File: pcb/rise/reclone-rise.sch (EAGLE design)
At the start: 3 parts, among them U1 6SLX25FTG256

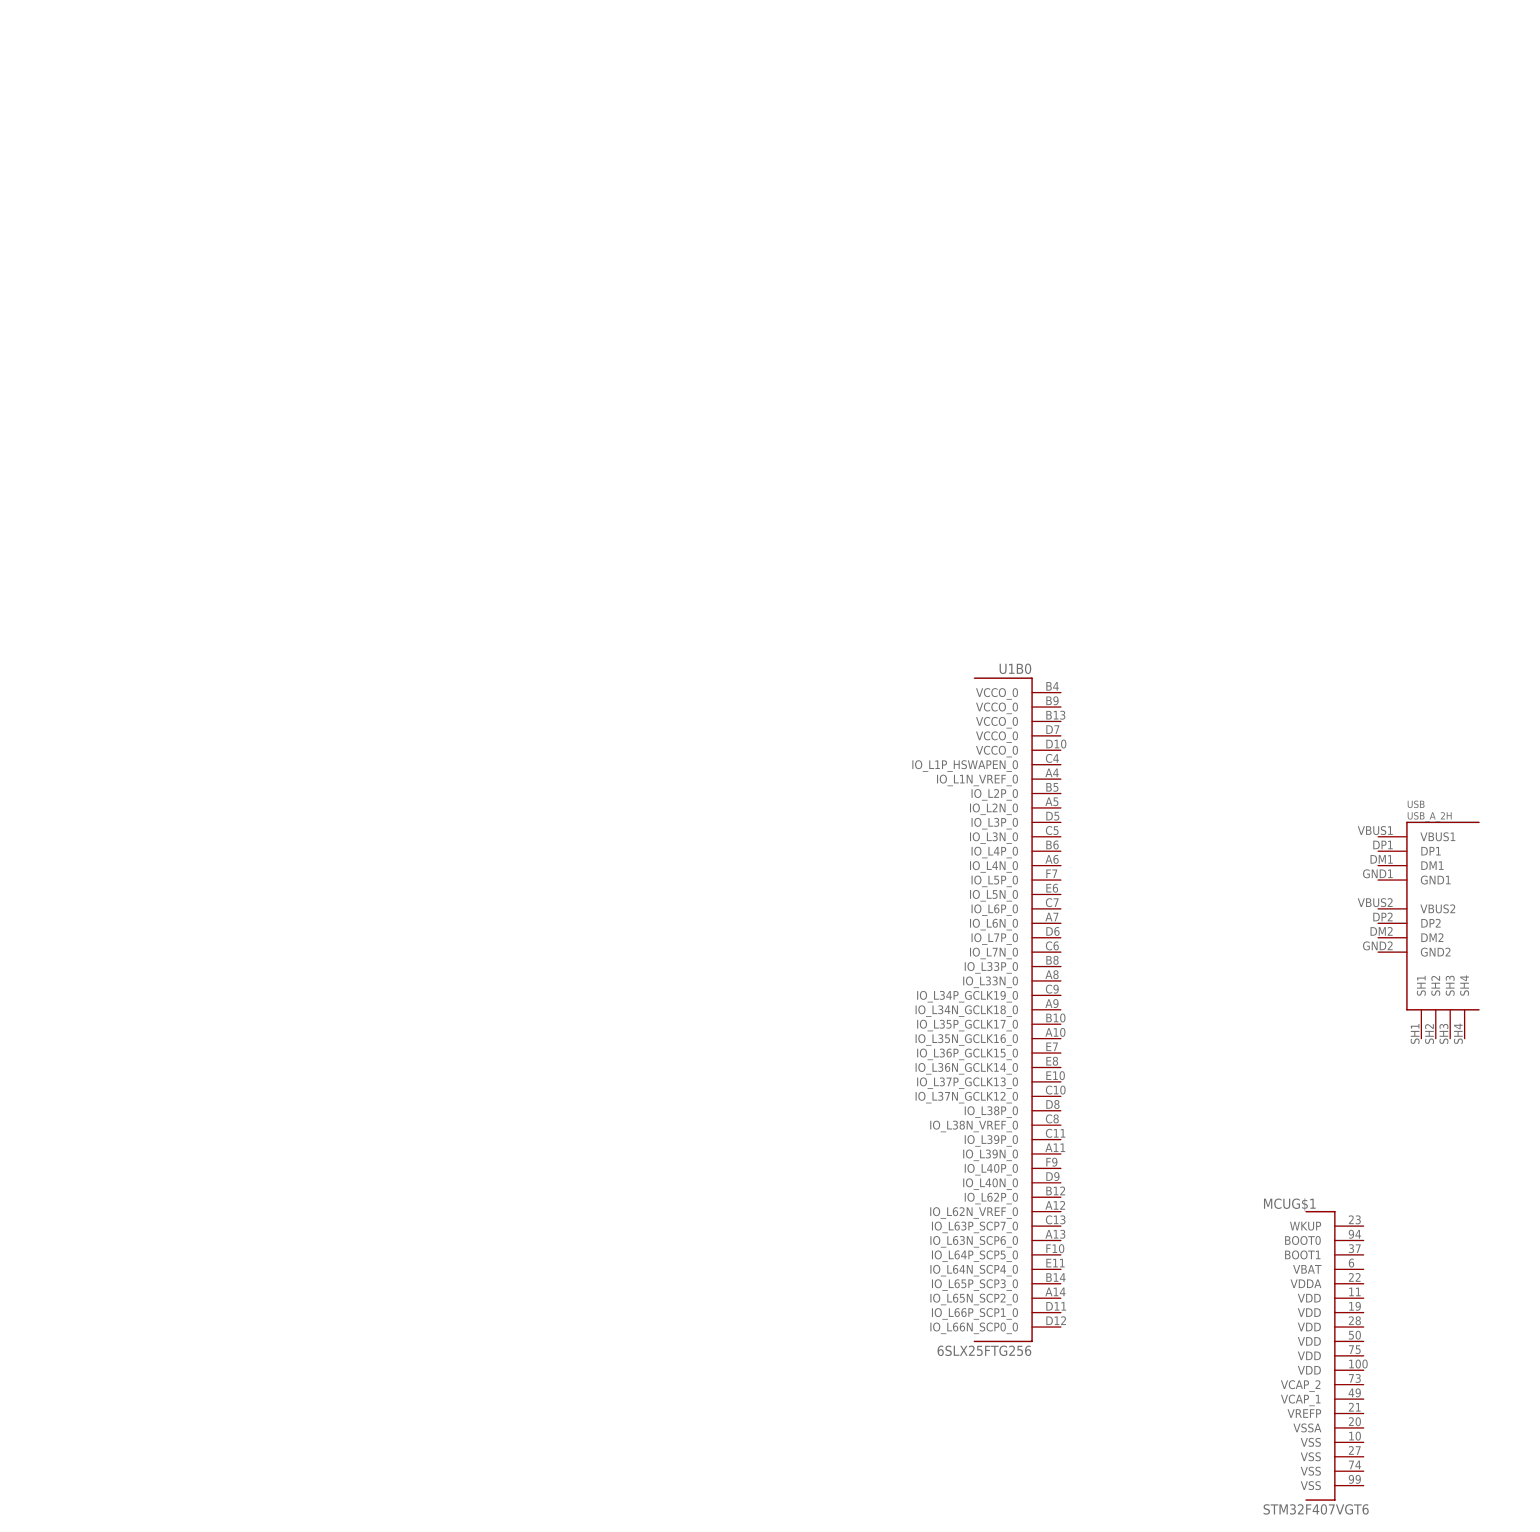
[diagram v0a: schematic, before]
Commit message: Added a ton of components just to get a sense for whether layout is possible on the top of the board
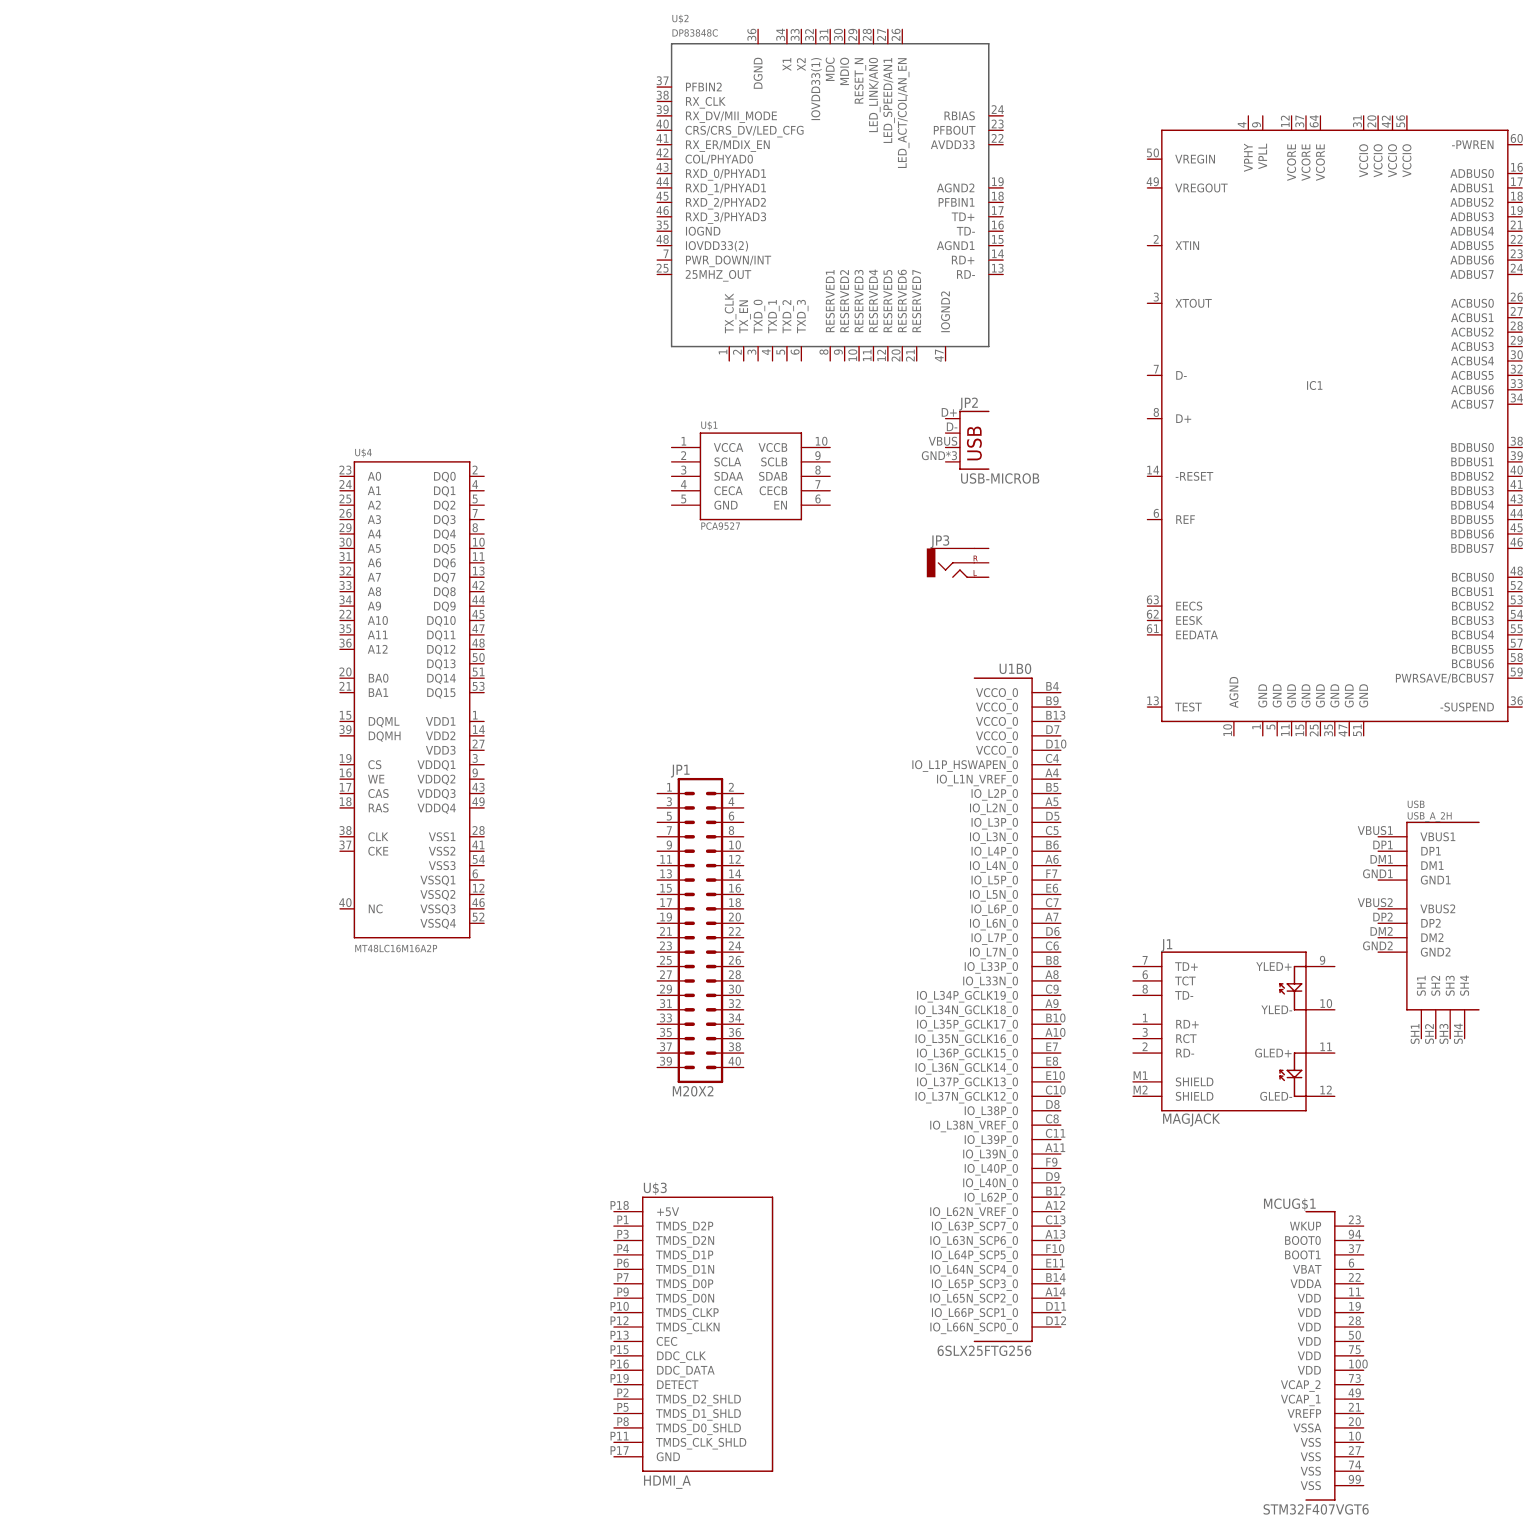
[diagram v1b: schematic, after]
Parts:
- added IC1: (no value), ftdichip-3:FT2232HL
- added J1: MAGJACK, SparkFun-Connectors:MAGJACK
- added JP1: M20X2, SparkFun-Connectors:M20X2
- added JP2: USB-MICROB, SparkFun-Connectors:USB-MICROB
- added JP3: (no value), SparkFun-Connectors:AUDIO-JACKSMD2
- added U$1: PCA9527, reclone-rise:PCA9527
- added U$2: DP83848C, reclone-rise:DP83848C
- added U$3: HDMI_A, reclone-rise:HDMI_A
- added U$4: MT48LC16M16A2P, reclone-rise:MT48LC16M16A2P
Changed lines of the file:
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@@
 <part name="MCU" library="reclone-rise" deviceset="STM32F407VGT6" device=""/>
 <part name="U1" library="xilinx_devices_V6" deviceset="6SLX25FTG256" device=""/>
+<part name="JP1" library="SparkFun-Connectors" deviceset="M20X2" device=""/>
+<part name="J1" library="SparkFun-Connectors" deviceset="MAGJACK" device=""/>
+<part name="IC1" library="ftdichip-3" deviceset="FT2232H" device="L"/>
+<part name="JP2" library="SparkFun-Connectors" deviceset="USB" device="-MICROB"/>
+<part name="JP3" library="SparkFun-Connectors" deviceset="AUDIO-JACK" device="SMD2"/>
+<part name="U$1" library="reclone-rise" deviceset="PCA9527" device=""/>
+<part name="U$2" library="reclone-rise" deviceset="DP83848C" device=""/>
+<part name="U$3" library="reclone-rise" deviceset="HDMI_A" device=""/>
+<part name="U$4" library="reclone-rise" deviceset="MT48LC16M16A2P" device=""/>
 </parts>
 <sheets>
@@
 <instance part="MCU" gate="G$1" x="50.8" y="-2.54"/>
 <instance part="U1" gate="B0" x="2.54" y="83.82"/>
+<instance part="JP1" gate="G$1" x="-55.88" y="99.06"/>
+<instance part="J1" gate="G$1" x="38.1" y="81.28"/>
+<instance part="IC1" gate="G$1" x="55.88" y="193.04"/>
+<instance part="JP2" gate="G$1" x="-10.16" y="180.34"/>
+<instance part="JP3" gate="G$1" x="-10.16" y="162.56"/>
+<instance part="U$1" gate="G$1" x="-45.72" y="177.8"/>
+<instance part="U$2" gate="G$1" x="-33.02" y="228.6"/>
+<instance part="U$3" gate="G$1" x="-55.88" y="27.94"/>
+<instance part="U$4" gate="G$1" x="-106.68" y="137.16"/>
 </instances>
 <busses>

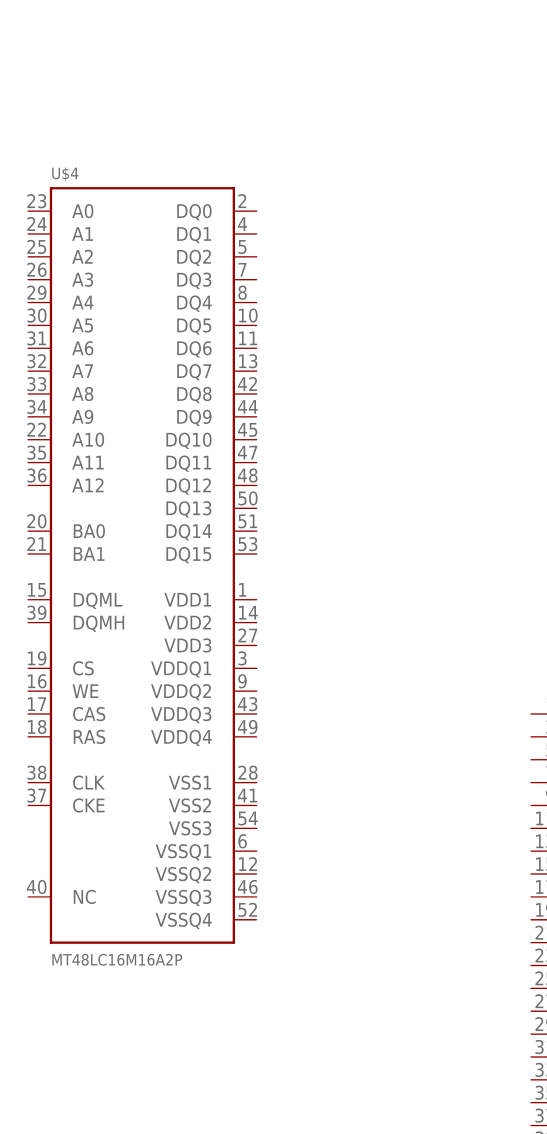
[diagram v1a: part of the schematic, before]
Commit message: Added rectangle to help plan for the size of a DDR2 chip
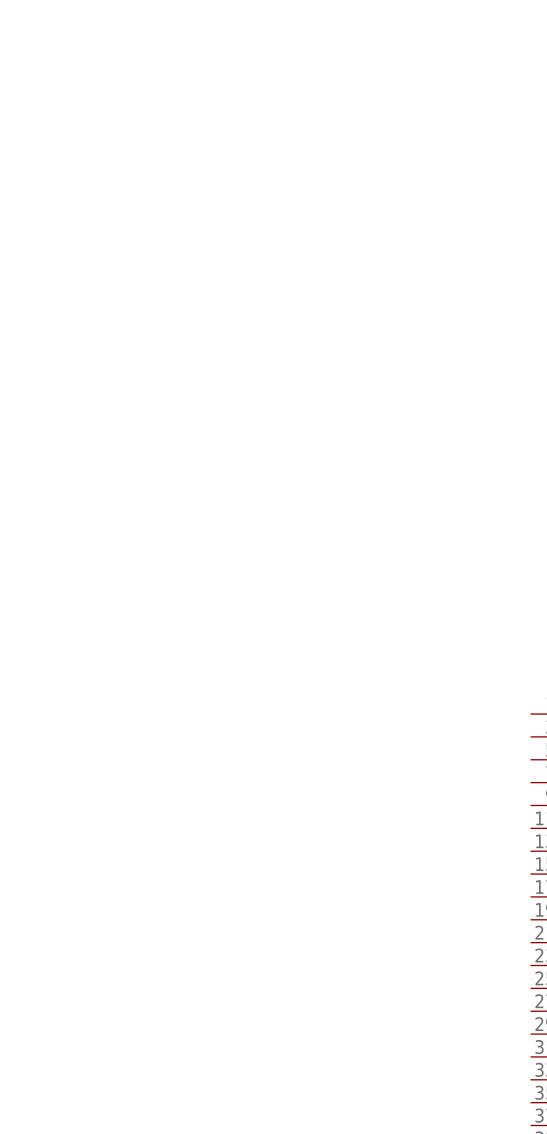
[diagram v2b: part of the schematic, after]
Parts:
- removed U$4: MT48LC16M16A2P, reclone-rise:MT48LC16M16A2P
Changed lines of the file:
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@@
 <part name="U$2" library="reclone-rise" deviceset="DP83848C" device=""/>
 <part name="U$3" library="reclone-rise" deviceset="HDMI_A" device=""/>
-<part name="U$4" library="reclone-rise" deviceset="MT48LC16M16A2P" device=""/>
 </parts>
 <sheets>
@@
 <instance part="U$2" gate="G$1" x="-33.02" y="228.6"/>
 <instance part="U$3" gate="G$1" x="-55.88" y="27.94"/>
-<instance part="U$4" gate="G$1" x="-106.68" y="137.16"/>
 </instances>
 <busses>

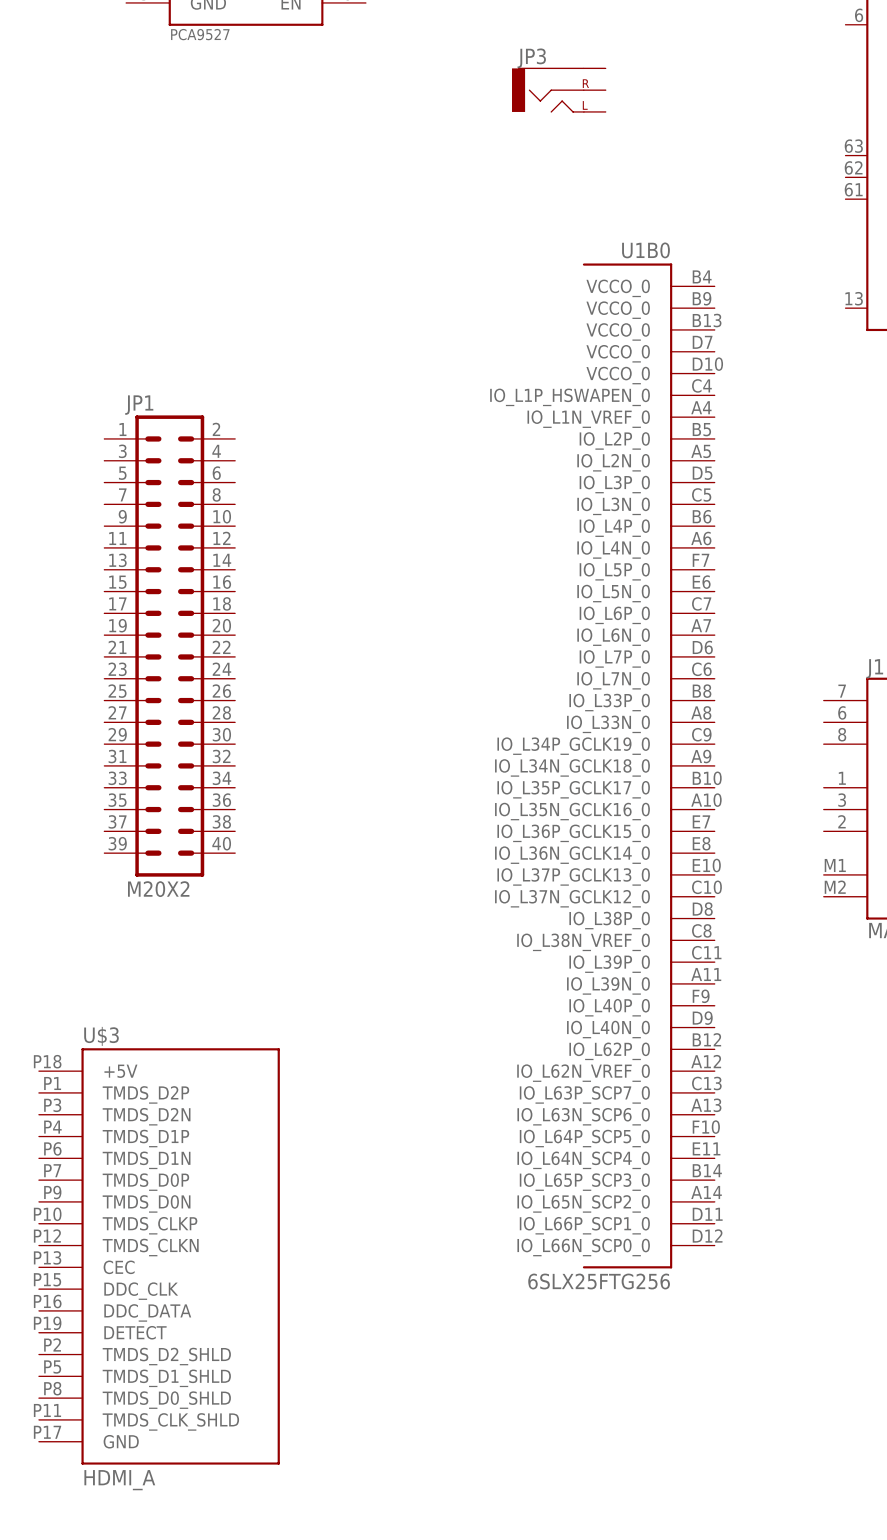
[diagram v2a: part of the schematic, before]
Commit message: Added Gadgeteer socket
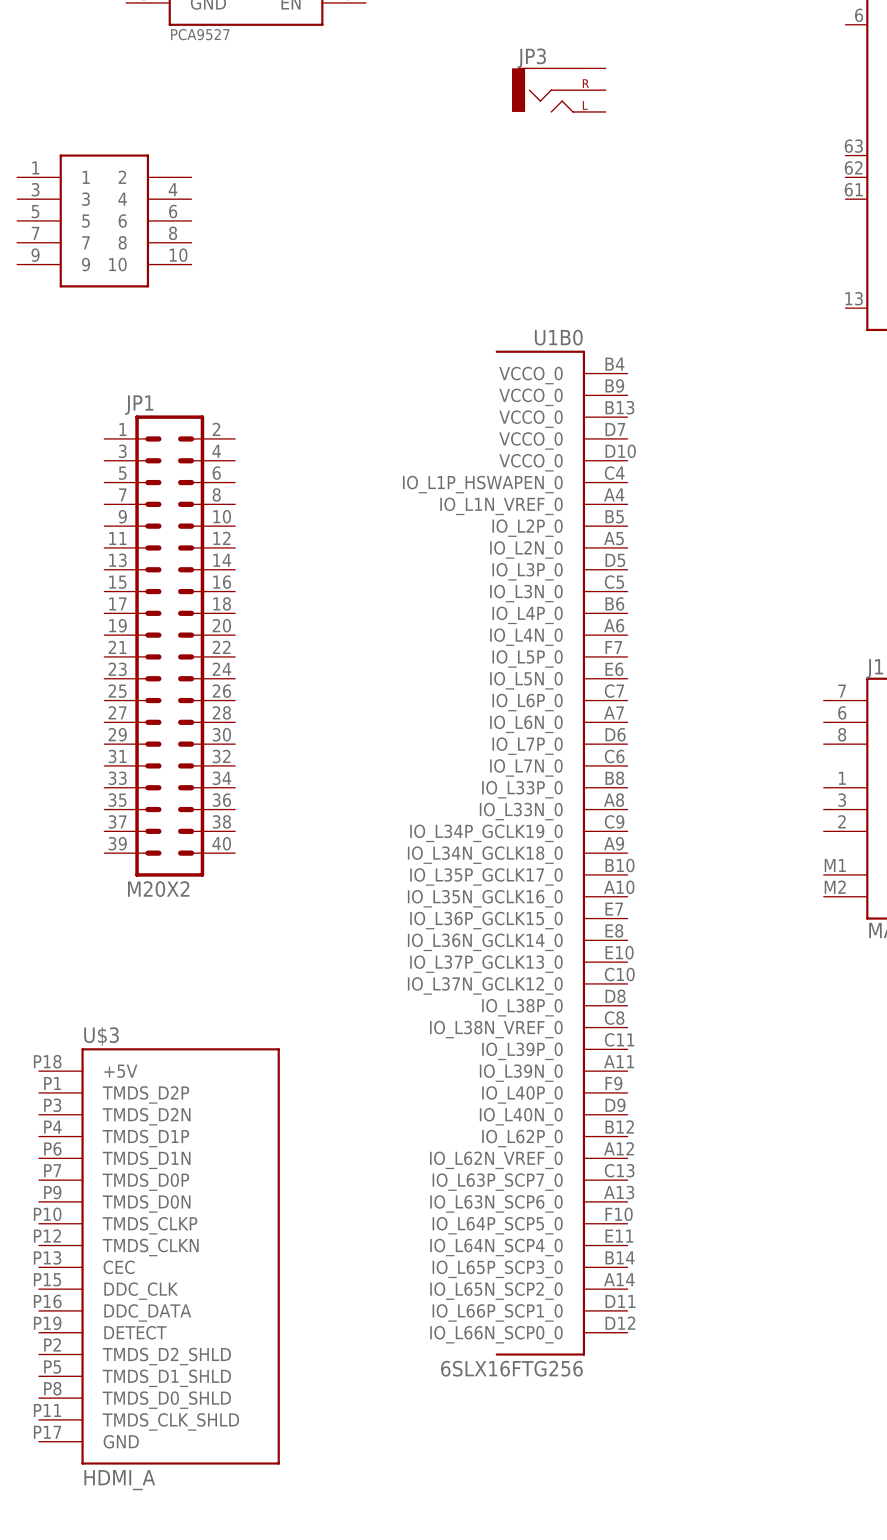
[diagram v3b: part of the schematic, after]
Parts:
- added U$4: SHF105, Gadgeteer:SHF105
- U1: value 6SLX25FTG256 -> 6SLX16FTG256; device xilinx_devices_V6:6SLX25FTG256 -> xilinx_devices_V6:6SLX16FTG256
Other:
- moved on the sheet: U1B0
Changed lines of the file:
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@@
 <part name="USB" library="reclone-rise" deviceset="USB_A_2H" device=""/>
 <part name="MCU" library="reclone-rise" deviceset="STM32F407VGT6" device=""/>
-<part name="U1" library="xilinx_devices_V6" deviceset="6SLX25FTG256" device=""/>
 <part name="JP1" library="SparkFun-Connectors" deviceset="M20X2" device=""/>
 <part name="J1" library="SparkFun-Connectors" deviceset="MAGJACK" device=""/>
@@
 <part name="U$2" library="reclone-rise" deviceset="DP83848C" device=""/>
 <part name="U$3" library="reclone-rise" deviceset="HDMI_A" device=""/>
+<part name="U1" library="xilinx_devices_V6" deviceset="6SLX16FTG256" device=""/>
+<part name="U$4" library="Gadgeteer" deviceset="SHF105" device=""/>
 </parts>
 <sheets>
@@
 <instance part="USB" gate="USB_A_2H" x="68.58" y="99.06"/>
 <instance part="MCU" gate="G$1" x="50.8" y="-2.54"/>
-<instance part="U1" gate="B0" x="2.54" y="83.82"/>
 <instance part="JP1" gate="G$1" x="-55.88" y="99.06"/>
 <instance part="J1" gate="G$1" x="38.1" y="81.28"/>
@@
 <instance part="U$2" gate="G$1" x="-33.02" y="228.6"/>
 <instance part="U$3" gate="G$1" x="-55.88" y="27.94"/>
+<instance part="U1" gate="B0" x="-7.62" y="73.66"/>
+<instance part="U$4" gate="X" x="-63.5" y="147.32"/>
 </instances>
 <busses>
